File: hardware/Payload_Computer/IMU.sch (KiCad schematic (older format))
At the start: 9 parts, among them U1 BNO055, Y3 32.768kHz

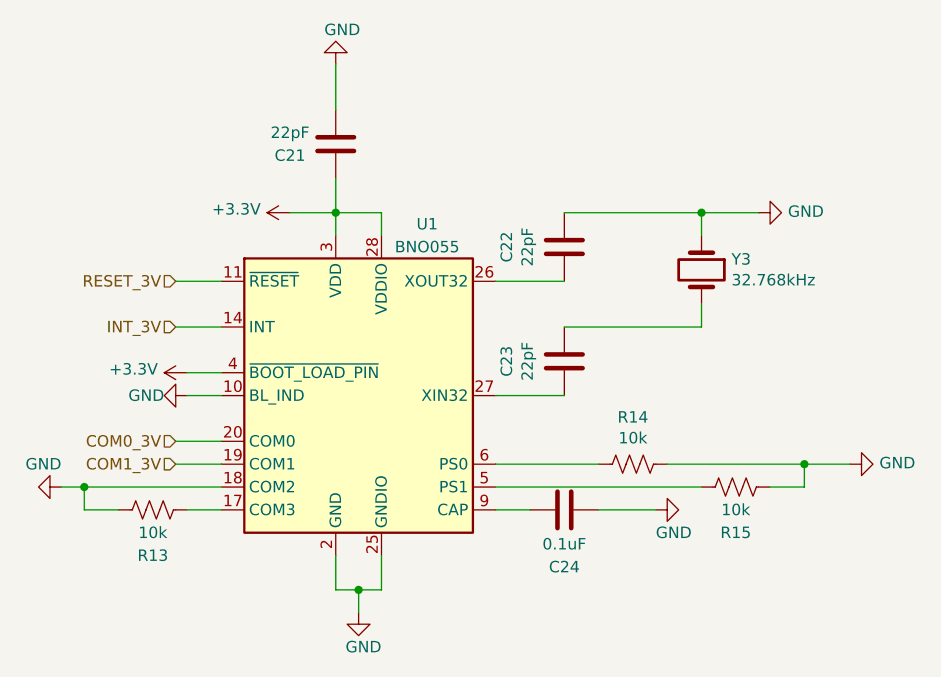
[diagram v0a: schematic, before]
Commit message: I'm dumb... changed CAPS on clock to parallel
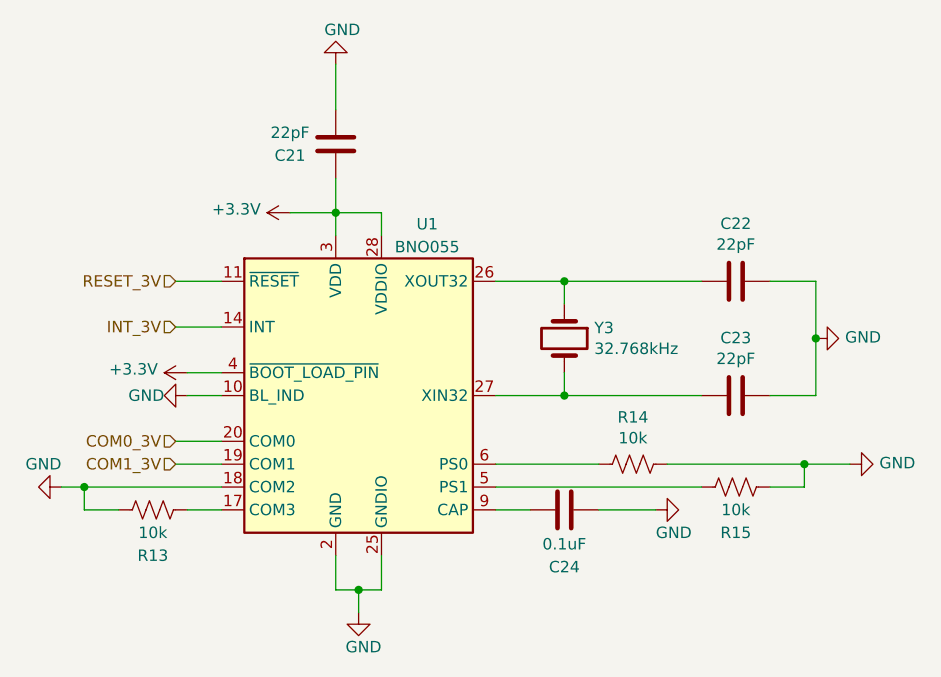
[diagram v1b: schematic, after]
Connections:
- net GND: now also C23.1; no longer Y3.1
- net at C22.2, U1.26 (XOUT32): now also Y3.1
- net at C23.2, U1.27 (XIN32): now also Y3.2
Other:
- moved on the sheet: C22, C23, Y3
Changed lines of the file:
@@
 	1    0    0    -1
 $EndComp
-Wire Wire Line
-	7450 3050 7700 3050
-Connection ~ 7450 3050
 $Comp
 L power:GND #PWR0143
 U 1 1 5FA09DDC
-P 7700 3050
-F 0 "#PWR0143" H 7700 2800 50  0001 C CNN
-F 1 "GND" V 7705 2922 50  0000 R CNN
-F 2 "" H 7700 3050 50  0001 C CNN
-F 3 "" H 7700 3050 50  0001 C CNN
-	1    7700 3050
+P 7950 3600
+F 0 "#PWR0143" H 7950 3350 50  0001 C CNN
+F 1 "GND" V 7955 3472 50  0000 R CNN
+F 2 "" H 7950 3600 50  0001 C CNN
+F 3 "" H 7950 3600 50  0001 C CNN
+	1    7950 3600
 	0    -1   -1   0
 $EndComp
@@
 L Device:C C22
 U 1 1 5FA09DE3
-P 6850 3200
-F 0 "C22" V 6598 3200 50  0000 C CNN
-F 1 "22pF" V 6689 3200 50  0000 C CNN
-F 2 "" H 6888 3050 50  0001 C CNN
-F 3 "~" H 6850 3200 50  0001 C CNN
-	1    6850 3200
-	1    0    0    -1
+P 7600 3350
+F 0 "C22" V 7348 3350 50  0000 C CNN
+F 1 "22pF" V 7439 3350 50  0000 C CNN
+F 2 "" H 7638 3200 50  0001 C CNN
+F 3 "~" H 7600 3350 50  0001 C CNN
+	1    7600 3350
+	0    1    1    0
 $EndComp
 $Comp
@@
 L Device:C C23
 U 1 1 5FA09E0D
-P 6850 3700
-F 0 "C23" V 6598 3700 50  0000 C CNN
-F 1 "22pF" V 6689 3700 50  0000 C CNN
-F 2 "" H 6888 3550 50  0001 C CNN
-F 3 "~" H 6850 3700 50  0001 C CNN
-	1    6850 3700
-	1    0    0    -1
+P 7600 3850
+F 0 "C23" V 7348 3850 50  0000 C CNN
+F 1 "22pF" V 7439 3850 50  0000 C CNN
+F 2 "" H 7638 3700 50  0001 C CNN
+F 3 "~" H 7600 3850 50  0001 C CNN
+	1    7600 3850
+	0    1    1    0
 $EndComp
 Wire Wire Line
@@
 Text HLabel 5150 4150 0    50   Input ~ 0
 COM1_3V
-Wire Wire Line
-	7450 3050 7450 3150
 $Comp
 L power:GND #PWR0151
@@
 L Device:Crystal Y3
 U 1 1 5FA09E67
-P 7450 3300
-F 0 "Y3" V 7404 3431 50  0000 L CNN
-F 1 "32.768kHz" V 7495 3431 50  0000 L CNN
-F 2 "" H 7450 3300 50  0001 C CNN
-F 3 "~" H 7450 3300 50  0001 C CNN
-	1    7450 3300
-	0    1    1    0
-$EndComp
-Wire Wire Line
-	7450 3450 7450 3550
+P 6850 3600
+F 0 "Y3" V 6804 3731 50  0000 L CNN
+F 1 "32.768kHz" V 6895 3731 50  0000 L CNN
+F 2 "" H 6850 3600 50  0001 C CNN
+F 3 "~" H 6850 3600 50  0001 C CNN
+	1    6850 3600
+	0    1    1    0
+$EndComp
 Wire Wire Line
 	6550 3350 6850 3350
@@
 	6550 3850 6850 3850
 Wire Wire Line
-	6850 3550 7450 3550
-Wire Wire Line
-	6850 3050 7450 3050
+	6850 3350 6850 3450
+Wire Wire Line
+	6850 3750 6850 3850
+Wire Wire Line
+	6850 3350 7450 3350
+Wire Wire Line
+	7950 3350 7950 3600
+Wire Wire Line
+	7950 3850 7750 3850
+Connection ~ 6850 3350
+Connection ~ 6850 3850
+Wire Wire Line
+	7450 3850 6850 3850
+Wire Wire Line
+	7750 3350 7950 3350
+Connection ~ 7950 3600
+Wire Wire Line
+	7950 3600 7950 3850
 $EndSCHEMATC

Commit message: Added a new processor. Fixed up some libraries. Did some schematic work.
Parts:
- renumbered C22 to C?, C24 to C?, C23 to C?, C21 to C?, R14 to R?, R15 to R?, R13 to R?, U1 to U?, Y3 to Y?
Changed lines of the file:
@@
 $Descr A4 11693 8268
 encoding utf-8
-Sheet 14 15
+Sheet 14 14
 Title ""
 Date ""
@@
 $EndDescr
 $Comp
-L Sensor_Motion:BNO055 U1
+L Sensor_Motion:BNO055 U?
 U 1 1 5FA09DD4
 P 5950 3850
-F 0 "U1" H 6250 4600 50  0000 C CNN
+F 0 "U?" H 6250 4600 50  0000 C CNN
 F 1 "BNO055" H 6250 4500 50  0000 C CNN
 F 2 "Package_LGA:LGA-28_5.2x3.8mm_P0.5mm" H 6200 3200 50  0001 L CNN
@@
 $EndComp
 $Comp
-L power:GND #PWR0143
+L power:GND #PWR?
 U 1 1 5FA09DDC
 P 7950 3600
-F 0 "#PWR0143" H 7950 3350 50  0001 C CNN
+F 0 "#PWR?" H 7950 3350 50  0001 C CNN
 F 1 "GND" V 7955 3472 50  0000 R CNN
 F 2 "" H 7950 3600 50  0001 C CNN
@@
 $EndComp
 $Comp
-L Device:C C22
+L Device:C C?
 U 1 1 5FA09DE3
 P 7600 3350
-F 0 "C22" V 7348 3350 50  0000 C CNN
+F 0 "C?" V 7348 3350 50  0000 C CNN
 F 1 "22pF" V 7439 3350 50  0000 C CNN
 F 2 "" H 7638 3200 50  0001 C CNN
@@
 $EndComp
 $Comp
-L Device:C C24
+L Device:C C?
 U 1 1 5FA09DE9
 P 6850 4350
-F 0 "C24" V 7100 4350 50  0000 C CNN
+F 0 "C?" V 7100 4350 50  0000 C CNN
 F 1 "0.1uF" V 7000 4350 50  0000 C CNN
 F 2 "" H 6888 4200 50  0001 C CNN
@@
 	7000 4350 7250 4350
 $Comp
-L Device:R_US R14
+L Device:R_US R?
 U 1 1 5FA09DF4
 P 7150 4150
-F 0 "R14" V 6945 4150 50  0000 C CNN
+F 0 "R?" V 6945 4150 50  0000 C CNN
 F 1 "10k" V 7036 4150 50  0000 C CNN
 F 2 "" V 7190 4140 50  0001 C CNN
@@
 $EndComp
 $Comp
-L Device:R_US R15
+L Device:R_US R?
 U 1 1 5FA09DFA
 P 7600 4250
-F 0 "R15" V 7800 4250 50  0000 C CNN
+F 0 "R?" V 7800 4250 50  0000 C CNN
 F 1 "10k" V 7700 4250 50  0000 C CNN
 F 2 "" V 7640 4240 50  0001 C CNN
@@
 Connection ~ 7900 4150
 $Comp
-L power:GND #PWR0144
+L power:GND #PWR?
 U 1 1 5FA09E07
 P 8100 4150
-F 0 "#PWR0144" H 8100 3900 50  0001 C CNN
+F 0 "#PWR?" H 8100 3900 50  0001 C CNN
 F 1 "GND" V 8105 4022 50  0000 R CNN
 F 2 "" H 8100 4150 50  0001 C CNN
@@
 $EndComp
 $Comp
-L Device:C C23
+L Device:C C?
 U 1 1 5FA09E0D
 P 7600 3850
-F 0 "C23" V 7348 3850 50  0000 C CNN
+F 0 "C?" V 7348 3850 50  0000 C CNN
 F 1 "22pF" V 7439 3850 50  0000 C CNN
 F 2 "" H 7638 3700 50  0001 C CNN
@@
 	5350 4250 4750 4250
 $Comp
-L power:GND #PWR0145
+L power:GND #PWR?
 U 1 1 5FA09E14
 P 4650 4250
-F 0 "#PWR0145" H 4650 4000 50  0001 C CNN
+F 0 "#PWR?" H 4650 4000 50  0001 C CNN
 F 1 "GND" V 4550 4250 50  0000 R CNN
 F 2 "" H 4650 4250 50  0001 C CNN
@@
 	4750 4250 4650 4250
 $Comp
-L Device:R_US R13
+L Device:R_US R?
 U 1 1 5FA09E1E
 P 5050 4350
-F 0 "R13" V 5250 4350 50  0000 C CNN
+F 0 "R?" V 5250 4350 50  0000 C CNN
 F 1 "10k" V 5150 4350 50  0000 C CNN
 F 2 "" V 5090 4340 50  0001 C CNN
@@
 	4900 4350 4750 4350
 $Comp
-L Device:C C21
+L Device:C C?
 U 1 1 5FA09E25
 P 5850 2750
-F 0 "C21" H 6050 2800 50  0000 C CNN
+F 0 "C?" H 6050 2800 50  0000 C CNN
 F 1 "22pF" H 6050 2700 50  0000 C CNN
 F 2 "" H 5888 2600 50  0001 C CNN
@@
 $EndComp
 $Comp
-L power:GND #PWR0146
+L power:GND #PWR?
 U 1 1 5FA09E2B
 P 5850 2400
-F 0 "#PWR0146" H 5850 2150 50  0001 C CNN
+F 0 "#PWR?" H 5850 2150 50  0001 C CNN
 F 1 "GND" H 5900 2250 50  0000 R CNN
 F 2 "" H 5850 2400 50  0001 C CNN
@@
 	5850 3050 5650 3050
 $Comp
-L power:+3.3V #PWR0147
+L power:+3.3V #PWR?
 U 1 1 5FA09E38
 P 5650 3050
-F 0 "#PWR0147" H 5650 2900 50  0001 C CNN
+F 0 "#PWR?" H 5650 2900 50  0001 C CNN
 F 1 "+3.3V" V 5665 3178 50  0000 L CNN
 F 2 "" H 5650 3050 50  0001 C CNN
@@
 	5950 4700 6050 4700
 $Comp
-L power:GND #PWR0148
+L power:GND #PWR?
 U 1 1 5FA09E44
 P 5950 4800
-F 0 "#PWR0148" H 5950 4550 50  0001 C CNN
+F 0 "#PWR?" H 5950 4550 50  0001 C CNN
 F 1 "GND" H 6050 4650 50  0000 R CNN
 F 2 "" H 5950 4800 50  0001 C CNN
@@
 	5350 3750 5200 3750
 $Comp
-L power:GND #PWR0149
+L power:GND #PWR?
 U 1 1 5FA09E4C
 P 5200 3850
-F 0 "#PWR0149" H 5200 3600 50  0001 C CNN
+F 0 "#PWR?" H 5200 3600 50  0001 C CNN
 F 1 "GND" V 5200 3750 50  0000 R CNN
 F 2 "" H 5200 3850 50  0001 C CNN
@@
 $EndComp
 $Comp
-L power:+3.3V #PWR0150
+L power:+3.3V #PWR?
 U 1 1 5FA09E52
 P 5200 3750
-F 0 "#PWR0150" H 5200 3600 50  0001 C CNN
+F 0 "#PWR?" H 5200 3600 50  0001 C CNN
 F 1 "+3.3V" V 5215 3878 50  0000 L CNN
 F 2 "" H 5200 3750 50  0001 C CNN
@@
 COM1_3V
 $Comp
-L power:GND #PWR0151
+L power:GND #PWR?
 U 1 1 5FA09E61
 P 7250 4350
-F 0 "#PWR0151" H 7250 4100 50  0001 C CNN
+F 0 "#PWR?" H 7250 4100 50  0001 C CNN
 F 1 "GND" V 7150 4350 50  0000 R CNN
 F 2 "" H 7250 4350 50  0001 C CNN
@@
 $EndComp
 $Comp
-L Device:Crystal Y3
+L Device:Crystal Y?
 U 1 1 5FA09E67
 P 6850 3600
-F 0 "Y3" V 6804 3731 50  0000 L CNN
+F 0 "Y?" V 6804 3731 50  0000 L CNN
 F 1 "32.768kHz" V 6895 3731 50  0000 L CNN
 F 2 "" H 6850 3600 50  0001 C CNN
